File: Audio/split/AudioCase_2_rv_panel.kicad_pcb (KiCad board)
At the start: 2 copper layers, 79.3 x 56.6 mm, 46 parts, among them J6 AUX_IN, J7 V_IN, J8 AUX_OUT, U2 NJM4558, U3 NJM4558

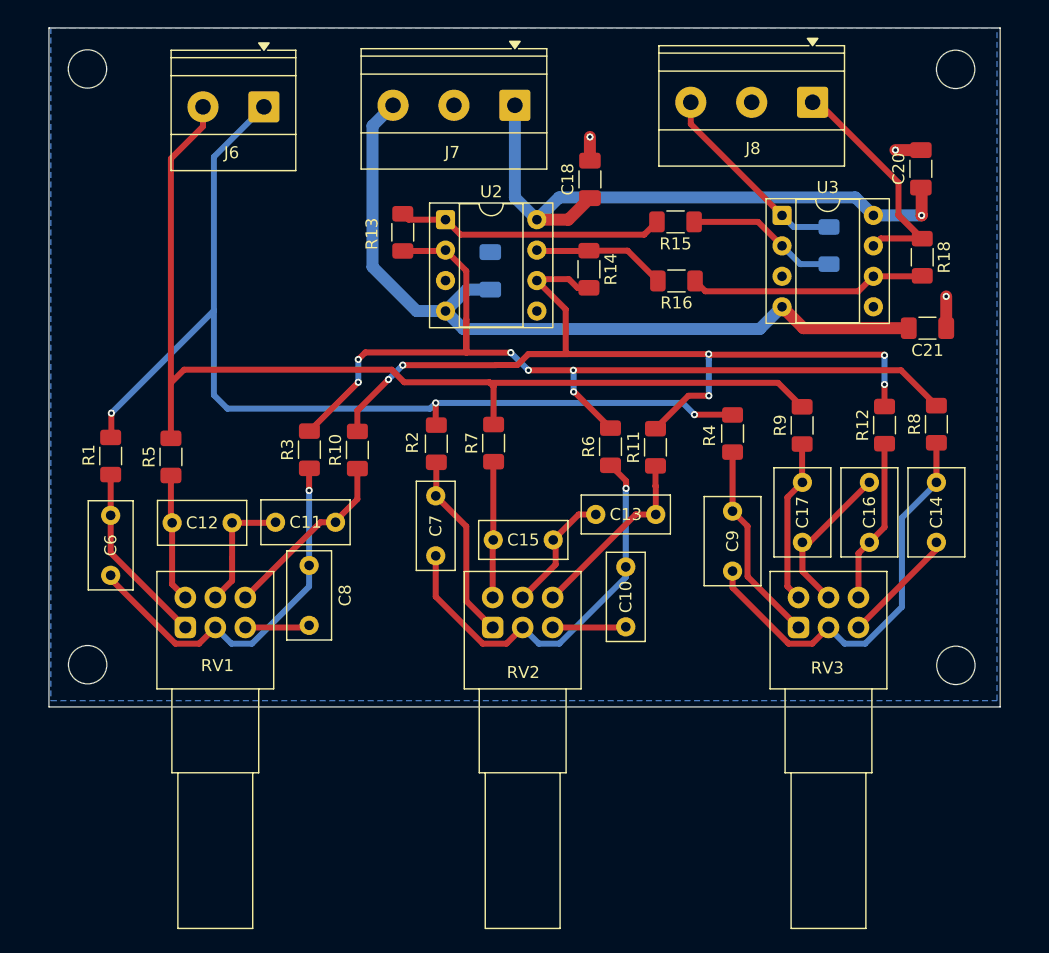
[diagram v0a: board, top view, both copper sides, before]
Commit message: ノイズ対策と製造データ整備: デカップリング追加・GNDベタ強化・シルク整理
- 5V_+ラインにデカップリング/バルク(C34-C37)を追加し、リレー切替時の電源変動を抑制
- F.CuにCTRL_GND/GNDベタを追加し、ステッチングビアで表裏GNDを補強(DC-DC周辺含む)
- 端子台ラベル等のシルク重なりを解消(J11/J14/J6/J4/L1/L2ほか)
- masterから4基板を再split、Gerber/zipを再生成

Co-authored-by: Cursor <cursoragent@cursor.com>
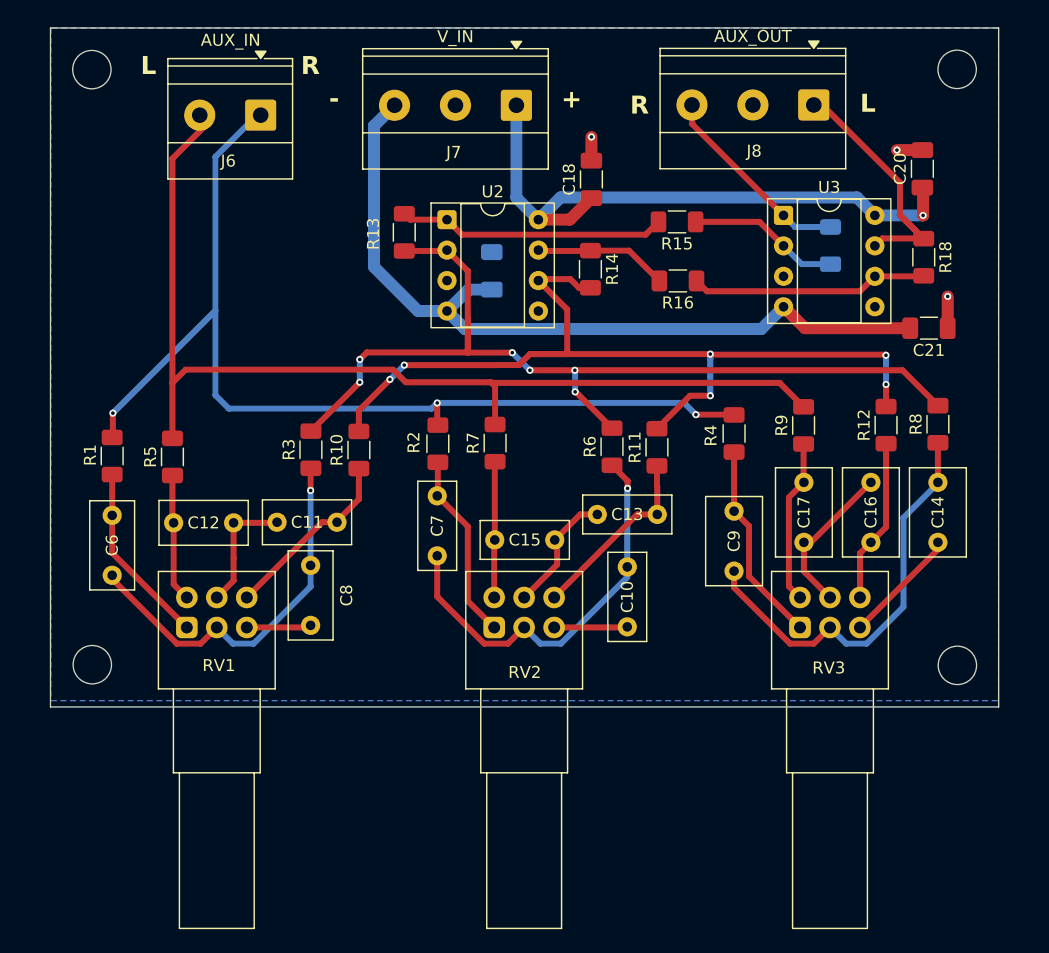
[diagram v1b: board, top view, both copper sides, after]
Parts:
- moved J6 0.75 mm to (126.5, 27.3)
- moved H8 0.39 mm to (112.4, 73.1)
- moved H5 0.37 mm to (112.4, 23.5)
- moved J8 0.25 mm to (172.6, 26.4)
- moved C10 0.12 mm to (157.1, 65.0)
- moved C11 0.12 mm to (132.9, 61.2)
- moved C12 0.12 mm to (124.2, 61.3)
- moved C13 0.12 mm to (159.6, 60.6)
- moved C14 0.12 mm to (183.0, 57.9)
- moved C15 0.12 mm to (151.0, 62.7)
- moved C16 0.12 mm to (177.4, 62.9)
- moved C17 0.12 mm to (171.8, 62.9)
- moved C18 0.12 mm to (154.1, 32.6)
- moved C19 0.12 mm to (145.8, 40.3)
- moved C20 0.12 mm to (181.7, 31.8)
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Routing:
- net /EQModule/R_IN: track 86.1 -> 85.5 mm
- net /EQModule/L_IN: track 86.7 -> 86.2 mm
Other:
- board size 79.3 x 56.6 mm -> 79.1 x 56.6 mm
- board text added: "+"
- board text added: "-"
- board text added: "L"
- board text added: "R"

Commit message: AudioCaseのリレー・EQネット整理と分割Gerberを再生成する。
Controllでアンプ別リレーネットを分離し、EQのバッファ入力をL/R_BUFF_INに改名。4枚分割PCBと発注用Gerberを更新し、RVパネルKiKit矩形とmacOS向けツール探索も修正。

Co-authored-by: Cursor <cursoragent@cursor.com>
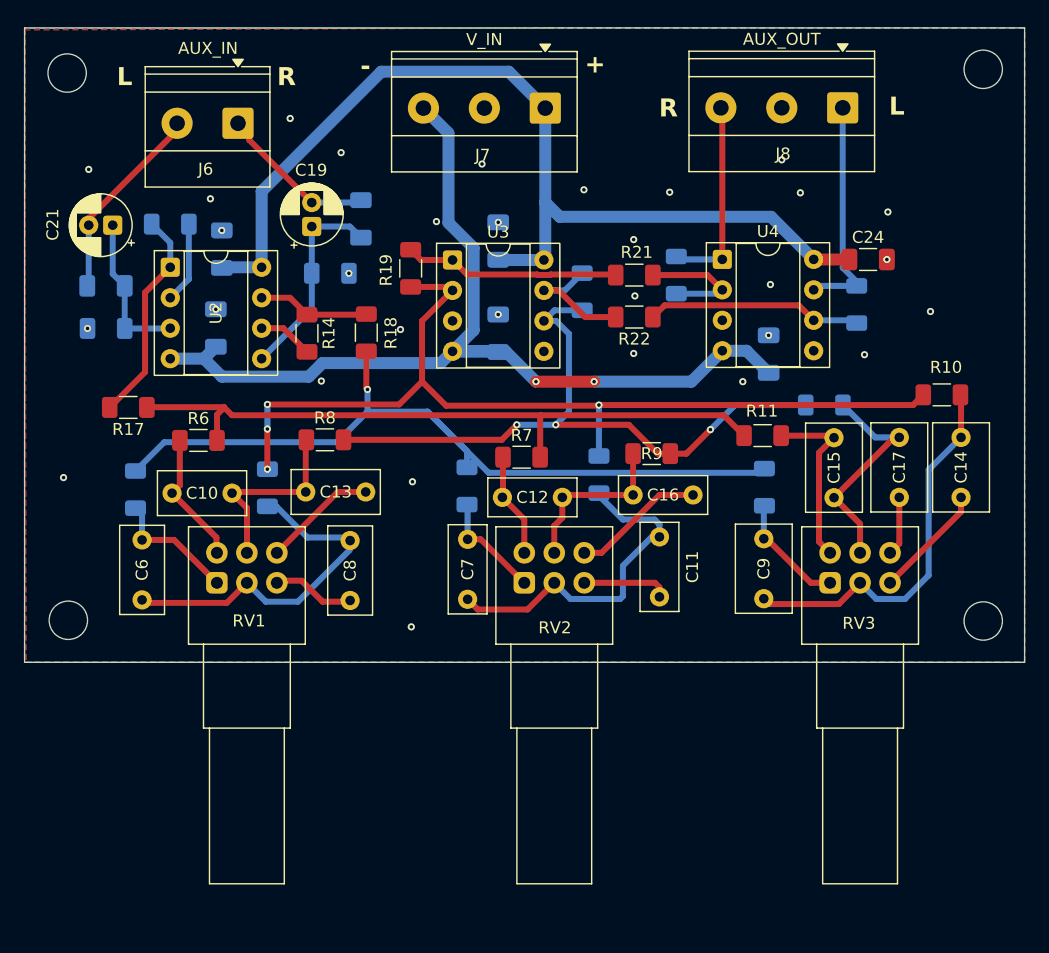
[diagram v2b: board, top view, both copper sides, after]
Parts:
- added C22: 0.1μF, Capacitor_SMD:C_1206_3216Metric_Pad1.33x1.80mm_HandSolder, B.Cu at (146.3, 37.8)
- added C23: 0.1μF, Capacitor_SMD:C_1206_3216Metric_Pad1.33x1.80mm_HandSolder, B.Cu at (146.3, 45.5)
- added C24: 0.1μF, Capacitor_SMD:C_1206_3216Metric_Pad1.33x1.80mm_HandSolder, F.Cu at (177.2, 39.3)
- added C25: 0.1μF, Capacitor_SMD:C_1206_3216Metric_Pad1.33x1.80mm_HandSolder, B.Cu at (168.8, 47.2)
- added C26: 0.1μF, Capacitor_SMD:C_1206_3216Metric_Pad1.33x1.80mm_HandSolder, B.Cu at (123.2, 38.5)
- added C27: 0.1μF, Capacitor_SMD:C_1206_3216Metric_Pad1.33x1.80mm_HandSolder, B.Cu at (122.8, 45.0)
- added R19: 10KΩ, Resistor_SMD:R_1206_3216Metric_Pad1.30x1.75mm_HandSolder, F.Cu at (139.0, 40.0)
- added R20: 10KΩ, Resistor_SMD:R_1206_3216Metric_Pad1.30x1.75mm_HandSolder, B.Cu at (153.3, 42.0)
- added R21: 22KΩ, Resistor_SMD:R_1206_3216Metric_Pad1.30x1.75mm_HandSolder, F.Cu at (157.7, 40.6)
- added R22: 22KΩ, Resistor_SMD:R_1206_3216Metric_Pad1.30x1.75mm_HandSolder, F.Cu at (157.7, 44.1)
- added R23: 22KΩ, Resistor_SMD:R_1206_3216Metric_Pad1.30x1.75mm_HandSolder, B.Cu at (161.2, 40.6)
- added R24: 22KΩ, Resistor_SMD:R_1206_3216Metric_Pad1.30x1.75mm_HandSolder, B.Cu at (176.2, 43.1)
- added U4: NJM4558, Package_DIP:DIP-8_W7.62mm_Socket, F.Cu at (165.0, 39.3)
- C10, C13: value 0.01uF -> 0.047μF; footprint Capacitor_THT:C_Rect_L7.2mm_W3.0mm_P5.00mm_FKS2_FKP2_MKS2_MKP2 -> Capacitor_THT:C_Rect_L7.2mm_W3.5mm_P5.00mm_FKS2_FKP2_MKS2_MKP2
- C11, C12: value 0.047μF -> 0.01uF; footprint Capacitor_THT:C_Rect_L7.2mm_W3.5mm_P5.00mm_FKS2_FKP2_MKS2_MKP2 -> Capacitor_THT:C_Rect_L7.2mm_W3.0mm_P5.00mm_FKS2_FKP2_MKS2_MKP2
- C15: value 0.01uF -> 2200pF; footprint Capacitor_THT:C_Rect_L7.2mm_W3.0mm_P5.00mm_FKS2_FKP2_MKS2_MKP2 -> Capacitor_THT:C_Rect_L7.2mm_W4.5mm_P5.00mm_FKS2_FKP2_MKS2_MKP2
- C16: value 2200pF -> 0.01uF; footprint Capacitor_THT:C_Rect_L7.2mm_W4.5mm_P5.00mm_FKS2_FKP2_MKS2_MKP2 -> Capacitor_THT:C_Rect_L7.2mm_W3.0mm_P5.00mm_FKS2_FKP2_MKS2_MKP2
- C18, C20, R1, R12, R2, R3, R4, R5: moved to B.Cu
- C19: value 0.1μF -> 10μF; footprint Capacitor_SMD:C_1206_3216Metric_Pad1.33x1.80mm_HandSolder -> Capacitor_THT:CP_Radial_D5.0mm_P2.00mm; moved to F.Cu
- C21: value 0.1μF -> 10μF; footprint Capacitor_SMD:C_1206_3216Metric_Pad1.33x1.80mm_HandSolder -> Capacitor_THT:CP_Radial_D5.0mm_P2.00mm
- R13: value 10KΩ -> 0Ω; moved to B.Cu
- R14: value 10KΩ -> 0Ω
- R15, R16: value 22KΩ -> 47kΩ; moved to B.Cu
- R17: value 22KΩ -> 47Ω; moved to F.Cu
- R18: value 22KΩ -> 47Ω
- moved C20 68.8 mm to (113.6, 41.5), turned to 180 degrees
- moved C21 68.6 mm to (114.2, 36.5)
- moved R17 60.1 mm to (115.5, 51.6), turned to 180 degrees
- moved R8 51.1 mm to (131.8, 54.4), turned to 0 degrees
- moved R5 49.4 mm to (168.5, 58.3), turned to -90 degrees
- moved R10 48.8 mm to (183.3, 50.6), turned to 180 degrees
- moved R16 47.9 mm to (113.6, 45.1)
- moved R18 46.9 mm to (135.3, 45.4), turned to 90 degrees
- moved R6 34.5 mm to (121.3, 54.4), turned to 0 degrees
- moved C10 33.5 mm to (124.1, 58.8), turned to 180 degrees
- moved R15 29.2 mm to (132.3, 40.5), turned to 0 degrees
- moved U3 27.9 mm to (142.5, 39.4)
- moved C12 27.5 mm to (151.7, 59.1)
- moved C11 26.9 mm to (159.8, 62.5), turned to -90 degrees
- moved C13 24.4 mm to (135.2, 58.7)
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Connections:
- C12 pad 1: Net-(C11-Pad2) -> Net-(C12-Pad1)
- C13 pad 2: Net-(C13-Pad2) -> Net-(C10-Pad1)
- C15 pad 1: Net-(C13-Pad2) -> Net-(C15-Pad1)
- C16 pad 1: Net-(C16-Pad1) -> Net-(C12-Pad1)
- C17 pad 1: Net-(C16-Pad2) -> Net-(C15-Pad1)
- C18 pad 1: /Controll/AMP_V+_IN -> /EQModule/R_BUFF_IN
- C18 pad 2: GND -> /EQModule/R_IN
- C19 pad 1: GND -> /EQModule/R_BUFF_IN
- C19 pad 2: /Controll/AMP_V-_IN -> /EQModule/R_IN
- C20 pad 1: /Controll/AMP_V+_IN -> /EQModule/L_BUFF_IN
- C20 pad 2: GND -> /EQModule/L_IN
- C21 pad 1: GND -> /EQModule/L_BUFF_IN
- C21 pad 2: /Controll/AMP_V-_IN -> /EQModule/L_IN
- C7 pad 2: Net-(C10-Pad1) -> Net-(C11-Pad1)
- R1 pad 1: /EQModule/R_IN -> /EQModule/R_BUFF
- R10 pad 1: Net-(C11-Pad1) -> Net-(C14-Pad1)
- R10 pad 2: /EQModule/L_BAX_SUM -> /EQModule/R_BAX_SUM
- R11 pad 1: Net-(C13-Pad1) -> Net-(C15-Pad2)
- R11 pad 2: /EQModule/L_BAX_SUM -> /EQModule/L_BUFF
- R12 pad 1: Net-(C16-Pad1) -> Net-(C15-Pad1)
- R13 pad 2: /EQModule/R_BAX_SUM -> Net-(U2A--)
- R14 pad 2: /EQModule/L_BAX_SUM -> Net-(U2B--)
- R15 pad 1: Net-(U3A--) -> /EQModule/R_BUFF_IN
- R15 pad 2: Net-(R13-Pad1) -> GND
- R16 pad 1: Net-(U3B--) -> /EQModule/L_BUFF_IN
- R16 pad 2: Net-(R14-Pad1) -> GND
- R17 pad 1: /Controll/R_IN -> /EQModule/L_BUFF
- R17 pad 2: Net-(U3A--) -> Net-(R13-Pad1)
- R18 pad 1: /Controll/L_IN -> /EQModule/R_BUFF
- R18 pad 2: Net-(U3B--) -> Net-(R14-Pad1)
- R2 pad 1: /EQModule/R_IN -> /EQModule/R_BUFF
- R4 pad 1: /EQModule/R_IN -> Net-(C11-Pad1)
- R4 pad 2: Net-(C9-Pad1) -> /EQModule/R_BAX_SUM
- R5 pad 1: Net-(C12-Pad2) -> /EQModule/R_BUFF
- R5 pad 2: /EQModule/L_IN -> Net-(C9-Pad1)
- R6 pad 1: Net-(C10-Pad1) -> Net-(C10-Pad2)
- R6 pad 2: /EQModule/R_BAX_SUM -> /EQModule/L_BUFF
- R7 pad 1: Net-(C15-Pad2) -> Net-(C12-Pad2)
- R7 pad 2: /EQModule/L_IN -> /EQModule/L_BUFF
- R8 pad 1: Net-(C14-Pad1) -> Net-(C10-Pad1)
- R8 pad 2: /EQModule/R_BAX_SUM -> /EQModule/L_BAX_SUM
- R9 pad 1: Net-(C17-Pad2) -> Net-(C12-Pad1)
- R9 pad 2: /EQModule/L_IN -> /EQModule/L_BAX_SUM
- RV1 pad 4: Net-(C12-Pad2) -> Net-(C10-Pad2)
- RV1 pad 5: Net-(C11-Pad2) -> Net-(C10-Pad1)
- RV1 pad 6: Net-(C11-Pad1) -> Net-(C13-Pad1)
- RV2 pad 2: Net-(C10-Pad1) -> Net-(C11-Pad1)
- RV2 pad 3: Net-(C10-Pad2) -> Net-(C11-Pad2)
- RV2 pad 4: Net-(C15-Pad2) -> Net-(C12-Pad2)
- RV2 pad 5: Net-(C13-Pad2) -> Net-(C12-Pad1)
- RV2 pad 6: Net-(C13-Pad1) -> Net-(C16-Pad2)
- RV3 pad 4: Net-(C17-Pad2) -> Net-(C15-Pad2)
- RV3 pad 5: Net-(C16-Pad2) -> Net-(C15-Pad1)
- RV3 pad 6: Net-(C16-Pad1) -> Net-(C17-Pad2)
- U2 pad 2: /EQModule/R_BAX_SUM -> Net-(U2A--)
- U2 pad 3: GND -> /EQModule/L_BUFF_IN
- U2 pad 5: GND -> /EQModule/R_BUFF_IN
- U2 pad 6: /EQModule/L_BAX_SUM -> Net-(U2B--)
- U3 pad 1: /Controll/R_IN -> Net-(R19-Pad1)
- U3 pad 2: Net-(U3A--) -> /EQModule/R_BAX_SUM
- U3 pad 6: Net-(U3B--) -> /EQModule/L_BAX_SUM
- U3 pad 7: /Controll/L_IN -> Net-(R20-Pad1)
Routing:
- net /EQModule/R_IN: track 85.5 -> 13.3 mm, vias 3 -> 0
- net /EQModule/L_IN: track 86.2 -> 17.3 mm
- net /EQModule/R_BUFF: track 0.00 -> 68.0 mm, vias 0 -> 1
- net /EQModule/L_BUFF: track 0.00 -> 57.7 mm
- net /Controll/AMP_V+_IN: track 51.3 -> 82.6 mm, vias 1 -> 0
- net /EQModule/L_BAX_SUM: track 76.2 -> 55.9 mm, vias 6 -> 3
- net Net-(U3B--): track 19.8 -> 0.00 mm
- net Net-(C15-Pad1): track 0.00 -> 18.8 mm
- net Net-(R19-Pad1): track 0.00 -> 18.2 mm
- net Net-(C10-Pad1): track 34.2 -> 16.1 mm, vias 1 -> 0
- net Net-(U4B--): track 0.00 -> 18.0 mm
- net /EQModule/R_BUFF_IN: track 0.00 -> 17.4 mm
- net /Controll/AMP_V-_IN: track 66.6 -> 82.3 mm, vias 0 -> 2
- net Net-(C12-Pad1): track 0.00 -> 14.5 mm
- net Net-(C16-Pad1): track 13.7 -> 0.00 mm
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- added copper zone on F.Cu, net GND
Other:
- board size 79.1 x 56.6 mm -> 83.4 x 52.9 mm

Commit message: RVConvert基板を追加し、分割Gerber生成を5基板対応にする。
Co-authored-by: Cursor <cursoragent@cursor.com>
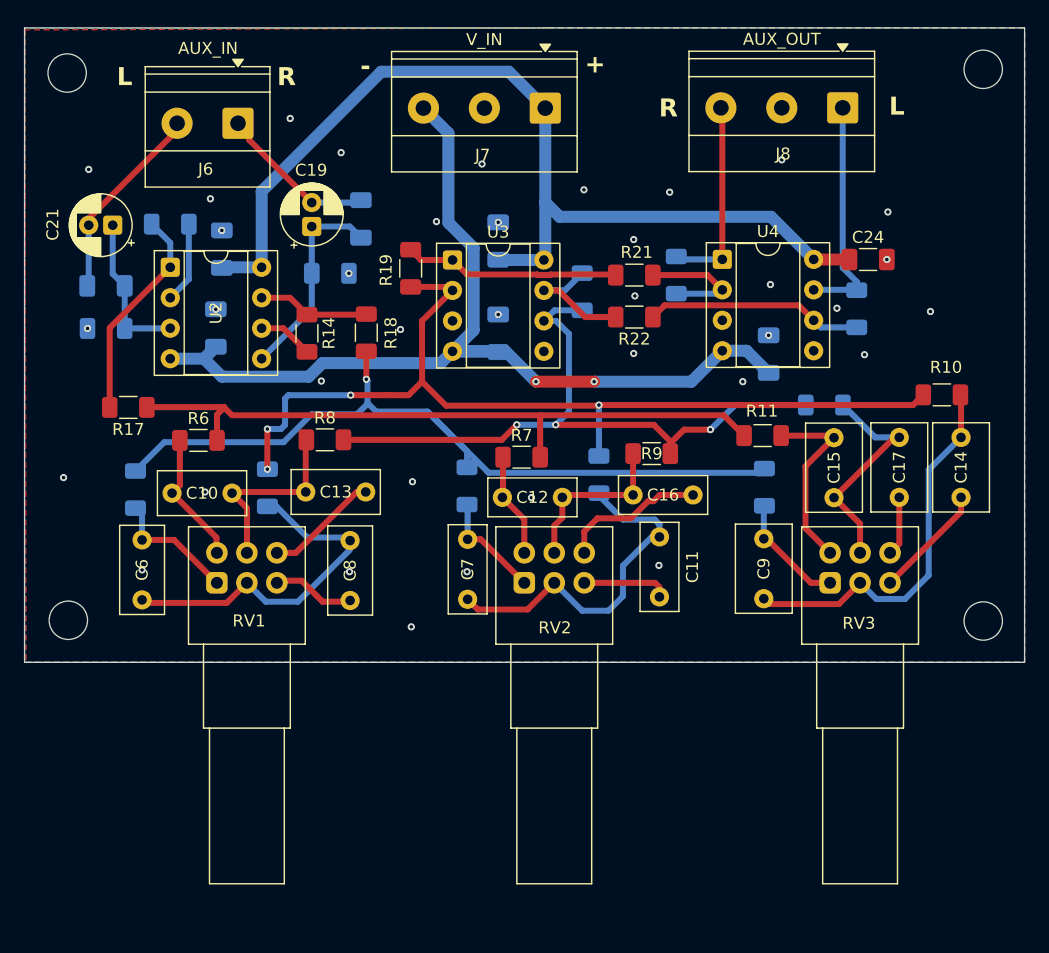
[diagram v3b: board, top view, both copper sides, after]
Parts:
- moved R24 0.36 mm to (176.2, 43.4)
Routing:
- net /EQModule/L_BAX_SUM: track 55.9 -> 57.0 mm
- net Net-(C16-Pad2): track 11.1 -> 12.2 mm
- net Net-(C15-Pad2): track 15.0 -> 15.9 mm
- net Net-(C11-Pad1): track 28.8 -> 29.6 mm
- net GND: vias 31 -> 37
